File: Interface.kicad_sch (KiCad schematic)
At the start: 20 parts

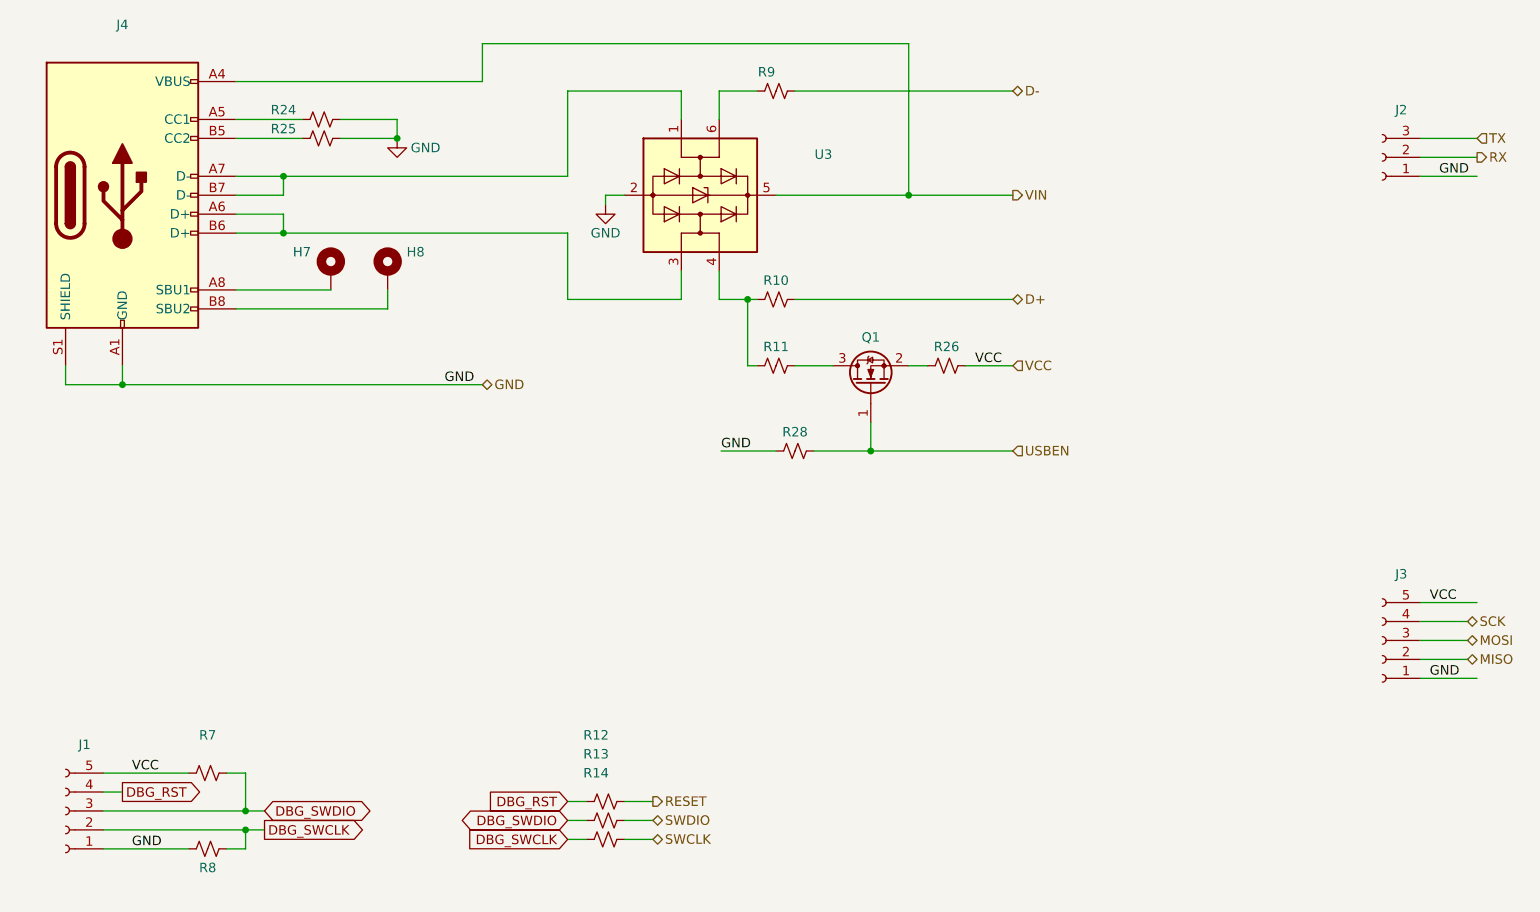
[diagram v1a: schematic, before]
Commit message: change Diode direction and update PR #1 footprint
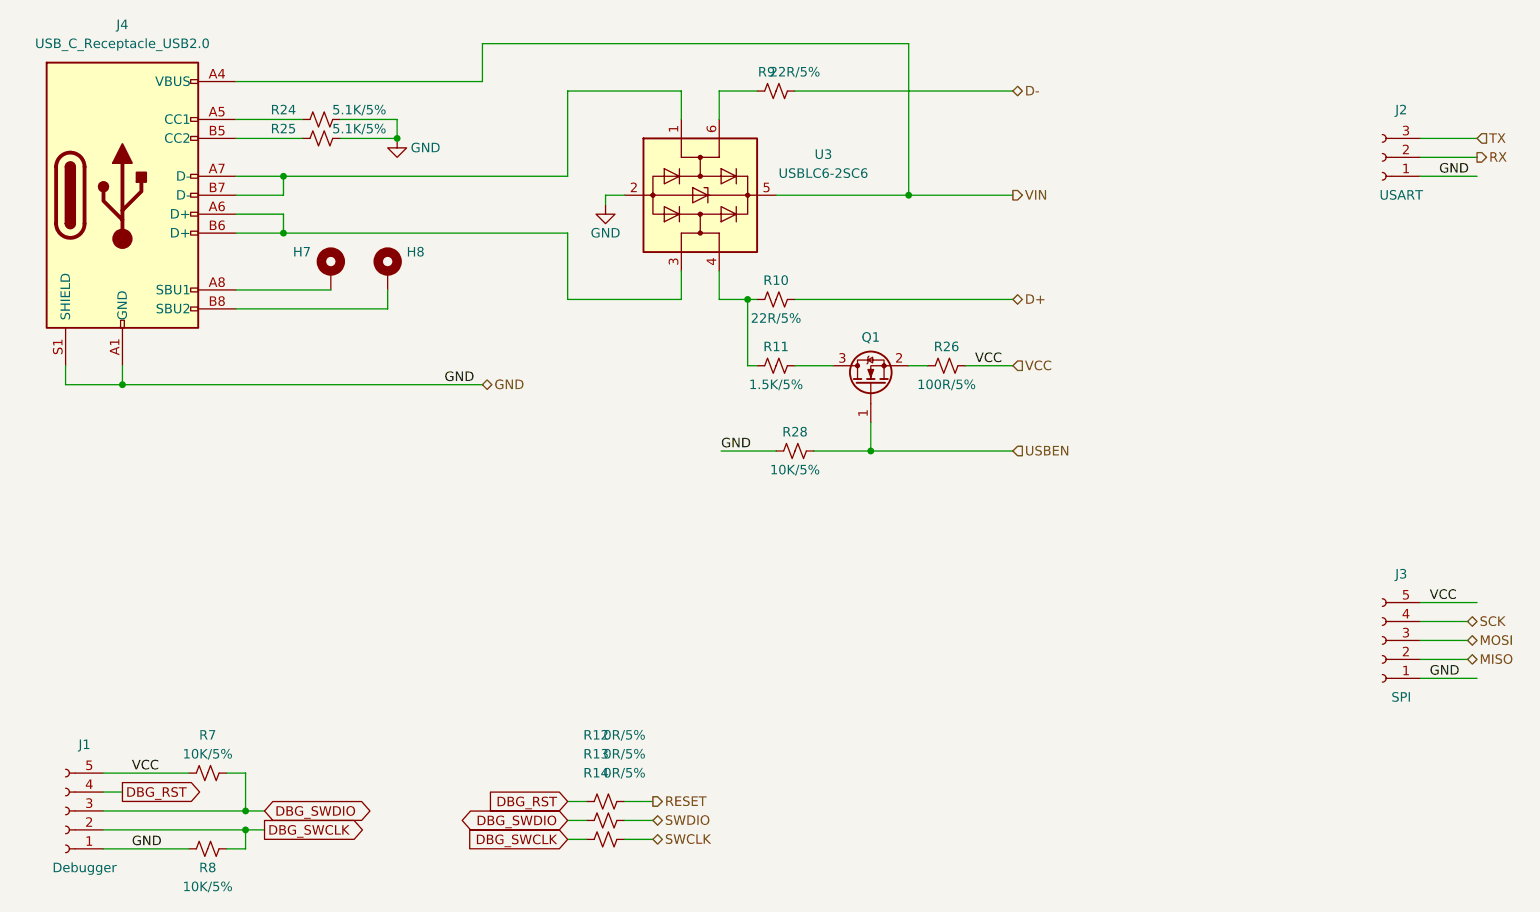
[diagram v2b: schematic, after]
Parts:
- H7, H8: value (none) -> MountingHole_Pad; footprint (none) -> NetTie:NetTie-2_SMD_Pad0.5mm
- J1: value (none) -> Debugger; footprint (none) -> Connector_PinHeader_2.00mm:PinHeader_1x05_P2.00mm_Vertical
- J2: value (none) -> USART; footprint (none) -> Connector_PinHeader_2.00mm:PinHeader_1x03_P2.00mm_Vertical
- J3: value (none) -> SPI; footprint (none) -> Connector_PinHeader_2.00mm:PinHeader_1x05_P2.00mm_Vertical
- J4: value (none) -> USB_C_Receptacle_USB2.0; footprint (none) -> Connector_USB:USB_C_Receptacle_HRO_TYPE-C-31-M-12
- Q1: value (none) -> Q_NMOS_GSD; footprint (none) -> Package_TO_SOT_SMD:SOT-23
- R10, R9: value (none) -> 22R/5%; footprint (none) -> Resistor_SMD:R_0603_1608Metric
- R11: value (none) -> 1.5K/5%; footprint (none) -> Resistor_SMD:R_0603_1608Metric
- R12, R13, R14: value (none) -> 0R/5%; footprint (none) -> Resistor_SMD:R_0603_1608Metric
- R24, R25: value (none) -> 5.1K/5%; footprint (none) -> Resistor_SMD:R_0603_1608Metric
- R26: value (none) -> 100R/5%; footprint (none) -> Resistor_SMD:R_0603_1608Metric
- R28, R7, R8: value (none) -> 10K/5%; footprint (none) -> Resistor_SMD:R_0603_1608Metric
- U3: value (none) -> USBLC6-2SC6; footprint (none) -> Package_TO_SOT_SMD:SOT-23-6
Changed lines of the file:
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@@
     (in_bom yes) (on_board yes)
     (property "Reference" "R25" (id 0) (at 77.47 44.45 90))
-    (property "Value" "" (id 1) (at 87.63 44.45 90))
-    (property "Footprint" "" (id 2) (at 82.55 45.72 0)
+    (property "Value" "5.1K/5%" (id 1) (at 87.63 44.45 90))
+    (property "Footprint" "Resistor_SMD:R_0603_1608Metric" (id 2) (at 82.55 45.72 0)
       (effects (font (size 1.27 1.27)) hide)
     )
@@
     (in_bom yes) (on_board yes) (fields_autoplaced)
     (property "Reference" "U3" (id 0) (at 149.86 47.8788 90))
-    (property "Value" "" (id 1) (at 149.86 50.4188 90))
-    (property "Footprint" "" (id 2) (at 120.65 53.34 0)
+    (property "Value" "USBLC6-2SC6" (id 1) (at 149.86 50.4188 90))
+    (property "Footprint" "Package_TO_SOT_SMD:SOT-23-6" (id 2) (at 120.65 53.34 0)
       (effects (font (size 1.27 1.27)) hide)
     )
@@
     (in_bom yes) (on_board yes)
     (property "Reference" "R8" (id 0) (at 67.31 143.51 90))
-    (property "Value" "" (id 1) (at 67.31 146.05 90))
-    (property "Footprint" "" (id 2) (at 67.31 140.97 0)
+    (property "Value" "10K/5%" (id 1) (at 67.31 146.05 90))
+    (property "Footprint" "Resistor_SMD:R_0603_1608Metric" (id 2) (at 67.31 140.97 0)
       (effects (font (size 1.27 1.27)) hide)
     )
@@
       (effects (font (size 1.27 1.27)) (justify left))
     )
-    (property "Value" "" (id 1) (at 86.36 63.4999 0)
+    (property "Value" "MountingHole_Pad" (id 1) (at 86.36 63.4999 0)
       (effects (font (size 1.27 1.27)) (justify left) hide)
     )
-    (property "Footprint" "" (id 2) (at 83.82 63.5 0)
+    (property "Footprint" "NetTie:NetTie-2_SMD_Pad0.5mm" (id 2) (at 83.82 63.5 0)
       (effects (font (size 1.27 1.27)) hide)
     )
@@
     (in_bom yes) (on_board yes)
     (property "Reference" "R11" (id 0) (at 143.51 73.66 90))
-    (property "Value" "" (id 1) (at 143.51 78.74 90))
-    (property "Footprint" "" (id 2) (at 143.51 76.2 0)
+    (property "Value" "1.5K/5%" (id 1) (at 143.51 78.74 90))
+    (property "Footprint" "Resistor_SMD:R_0603_1608Metric" (id 2) (at 143.51 76.2 0)
       (effects (font (size 1.27 1.27)) hide)
     )
@@
     (in_bom yes) (on_board yes)
     (property "Reference" "R14" (id 0) (at 119.38 130.81 90))
-    (property "Value" "" (id 1) (at 123.19 130.81 90))
-    (property "Footprint" "" (id 2) (at 120.65 139.7 0)
+    (property "Value" "0R/5%" (id 1) (at 123.19 130.81 90))
+    (property "Footprint" "Resistor_SMD:R_0603_1608Metric" (id 2) (at 120.65 139.7 0)
       (effects (font (size 1.27 1.27)) hide)
     )
@@
     (in_bom yes) (on_board yes)
     (property "Reference" "J3" (id 0) (at 227.33 104.14 0))
-    (property "Value" "" (id 1) (at 227.33 120.65 0))
-    (property "Footprint" "" (id 2) (at 224.79 113.03 0)
+    (property "Value" "SPI" (id 1) (at 227.33 120.65 0))
+    (property "Footprint" "Connector_PinHeader_2.00mm:PinHeader_1x05_P2.00mm_Vertical" (id 2) (at 224.79 113.03 0)
       (effects (font (size 1.27 1.27)) hide)
     )
@@
     (in_bom yes) (on_board yes)
     (property "Reference" "R24" (id 0) (at 77.47 41.91 90))
-    (property "Value" "" (id 1) (at 87.63 41.91 90))
-    (property "Footprint" "" (id 2) (at 82.55 43.18 0)
+    (property "Value" "5.1K/5%" (id 1) (at 87.63 41.91 90))
+    (property "Footprint" "Resistor_SMD:R_0603_1608Metric" (id 2) (at 82.55 43.18 0)
       (effects (font (size 1.27 1.27)) hide)
     )
@@
     (in_bom yes) (on_board yes)
     (property "Reference" "R26" (id 0) (at 166.37 73.66 90))
-    (property "Value" "" (id 1) (at 166.37 78.74 90))
-    (property "Footprint" "" (id 2) (at 166.37 76.2 0)
+    (property "Value" "100R/5%" (id 1) (at 166.37 78.74 90))
+    (property "Footprint" "Resistor_SMD:R_0603_1608Metric" (id 2) (at 166.37 76.2 0)
       (effects (font (size 1.27 1.27)) hide)
     )
@@
     (in_bom yes) (on_board yes)
     (property "Reference" "J1" (id 0) (at 50.8 127 0))
-    (property "Value" "" (id 1) (at 50.8 143.51 0))
-    (property "Footprint" "" (id 2) (at 48.26 135.89 0)
+    (property "Value" "Debugger" (id 1) (at 50.8 143.51 0))
+    (property "Footprint" "Connector_PinHeader_2.00mm:PinHeader_1x05_P2.00mm_Vertical" (id 2) (at 48.26 135.89 0)
       (effects (font (size 1.27 1.27)) hide)
     )
@@
     (in_bom yes) (on_board yes)
     (property "Reference" "R12" (id 0) (at 119.38 125.73 90))
-    (property "Value" "" (id 1) (at 123.19 125.73 90))
-    (property "Footprint" "" (id 2) (at 120.65 134.62 0)
+    (property "Value" "0R/5%" (id 1) (at 123.19 125.73 90))
+    (property "Footprint" "Resistor_SMD:R_0603_1608Metric" (id 2) (at 120.65 134.62 0)
       (effects (font (size 1.27 1.27)) hide)
     )
@@
     (in_bom yes) (on_board yes)
     (property "Reference" "R7" (id 0) (at 67.31 125.73 90))
-    (property "Value" "" (id 1) (at 67.31 128.27 90))
-    (property "Footprint" "" (id 2) (at 67.31 130.81 0)
+    (property "Value" "10K/5%" (id 1) (at 67.31 128.27 90))
+    (property "Footprint" "Resistor_SMD:R_0603_1608Metric" (id 2) (at 67.31 130.81 0)
       (effects (font (size 1.27 1.27)) hide)
     )
@@
     (in_bom yes) (on_board yes)
     (property "Reference" "R28" (id 0) (at 146.05 85.09 90))
-    (property "Value" "" (id 1) (at 146.05 90.17 90))
-    (property "Footprint" "" (id 2) (at 146.05 87.63 0)
+    (property "Value" "10K/5%" (id 1) (at 146.05 90.17 90))
+    (property "Footprint" "Resistor_SMD:R_0603_1608Metric" (id 2) (at 146.05 87.63 0)
       (effects (font (size 1.27 1.27)) hide)
     )
@@
     (in_bom yes) (on_board yes)
     (property "Reference" "J2" (id 0) (at 227.33 41.91 0))
-    (property "Value" "" (id 1) (at 227.33 53.34 0))
-    (property "Footprint" "" (id 2) (at 224.79 48.26 0)
+    (property "Value" "USART" (id 1) (at 227.33 53.34 0))
+    (property "Footprint" "Connector_PinHeader_2.00mm:PinHeader_1x03_P2.00mm_Vertical" (id 2) (at 224.79 48.26 0)
       (effects (font (size 1.27 1.27)) hide)
     )
@@
     (in_bom yes) (on_board yes)
     (property "Reference" "R13" (id 0) (at 119.38 128.27 90))
-    (property "Value" "" (id 1) (at 123.19 128.27 90))
-    (property "Footprint" "" (id 2) (at 120.65 137.16 0)
+    (property "Value" "0R/5%" (id 1) (at 123.19 128.27 90))
+    (property "Footprint" "Resistor_SMD:R_0603_1608Metric" (id 2) (at 120.65 137.16 0)
       (effects (font (size 1.27 1.27)) hide)
     )
@@
     (in_bom yes) (on_board yes)
     (property "Reference" "R9" (id 0) (at 142.24 36.83 90))
-    (property "Value" "" (id 1) (at 146.05 36.83 90))
-    (property "Footprint" "" (id 2) (at 143.51 39.37 0)
+    (property "Value" "22R/5%" (id 1) (at 146.05 36.83 90))
+    (property "Footprint" "Resistor_SMD:R_0603_1608Metric" (id 2) (at 143.51 39.37 0)
       (effects (font (size 1.27 1.27)) hide)
     )
@@
     (in_bom yes) (on_board yes)
     (property "Reference" "R10" (id 0) (at 143.51 64.77 90))
-    (property "Value" "" (id 1) (at 143.51 69.85 90))
-    (property "Footprint" "" (id 2) (at 143.51 67.31 0)
+    (property "Value" "22R/5%" (id 1) (at 143.51 69.85 90))
+    (property "Footprint" "Resistor_SMD:R_0603_1608Metric" (id 2) (at 143.51 67.31 0)
       (effects (font (size 1.27 1.27)) hide)
     )
@@
     (in_bom yes) (on_board yes) (fields_autoplaced)
     (property "Reference" "J4" (id 0) (at 55.88 30.48 0))
-    (property "Value" "" (id 1) (at 55.88 33.02 0))
-    (property "Footprint" "" (id 2) (at 59.69 53.34 0)
+    (property "Value" "USB_C_Receptacle_USB2.0" (id 1) (at 55.88 33.02 0))
+    (property "Footprint" "Connector_USB:USB_C_Receptacle_HRO_TYPE-C-31-M-12" (id 2) (at 59.69 53.34 0)
       (effects (font (size 1.27 1.27)) hide)
     )
@@
     (in_bom yes) (on_board yes)
     (property "Reference" "Q1" (id 0) (at 156.21 72.39 90))
-    (property "Value" "" (id 1) (at 156.21 71.12 90)
-      (effects (font (size 1.27 1.27)) hide)
-    )
-    (property "Footprint" "" (id 2) (at 153.67 73.66 0)
+    (property "Value" "Q_NMOS_GSD" (id 1) (at 156.21 71.12 90)
+      (effects (font (size 1.27 1.27)) hide)
+    )
+    (property "Footprint" "Package_TO_SOT_SMD:SOT-23" (id 2) (at 153.67 73.66 0)
       (effects (font (size 1.27 1.27)) hide)
     )
@@
       (effects (font (size 1.27 1.27)) (justify left))
     )
-    (property "Value" "" (id 1) (at 93.98 63.4999 0)
+    (property "Value" "MountingHole_Pad" (id 1) (at 93.98 63.4999 0)
       (effects (font (size 1.27 1.27)) (justify left) hide)
     )
-    (property "Footprint" "" (id 2) (at 91.44 63.5 0)
-      (effects (font (size 1.27 1.27)) hide)
-    )
+    (property "Footprint" "NetTie:NetTie-2_SMD_Pad0.5mm" (id 2) (at 91.44 63.5 0)
+      (effects (font (size 1.27 1.27)) hide)
+    )

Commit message: update pcb layout
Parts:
- removed Q1: Q_NMOS_GSD, Package_TO_SOT_SMD:SOT-23, symbol Device:Q_NMOS_GSD
- removed R11: 1.5K/5%, Resistor_SMD:R_0603_1608Metric, symbol Device:R_Small_US
- removed R14: 0R/5%, Resistor_SMD:R_0603_1608Metric, symbol Device:R_Small_US
- removed R26: 100R/5%, Resistor_SMD:R_0603_1608Metric, symbol Device:R_Small_US
- removed R28: 10K/5%, Resistor_SMD:R_0603_1608Metric, symbol Device:R_Small_US
- R13: value 0R/5% -> 1.5K/5%
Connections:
- net DBG_SWCLK is gone; now on net SWCLK: J1.2 (Pin_2), R8.2
- net D+: now also R13.1
- net SWDIO: now also J1.3 (Pin_3), R7.2; no longer R13.2
- net VCC: now also R13.2
- removed net DBG_SWDIO: J1.3 (Pin_3), R13.1, R7.2
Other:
- moved on the sheet: R12
